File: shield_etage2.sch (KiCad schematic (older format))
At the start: 8 parts, among them J1 Conn_01x02, J2 Conn_01x02

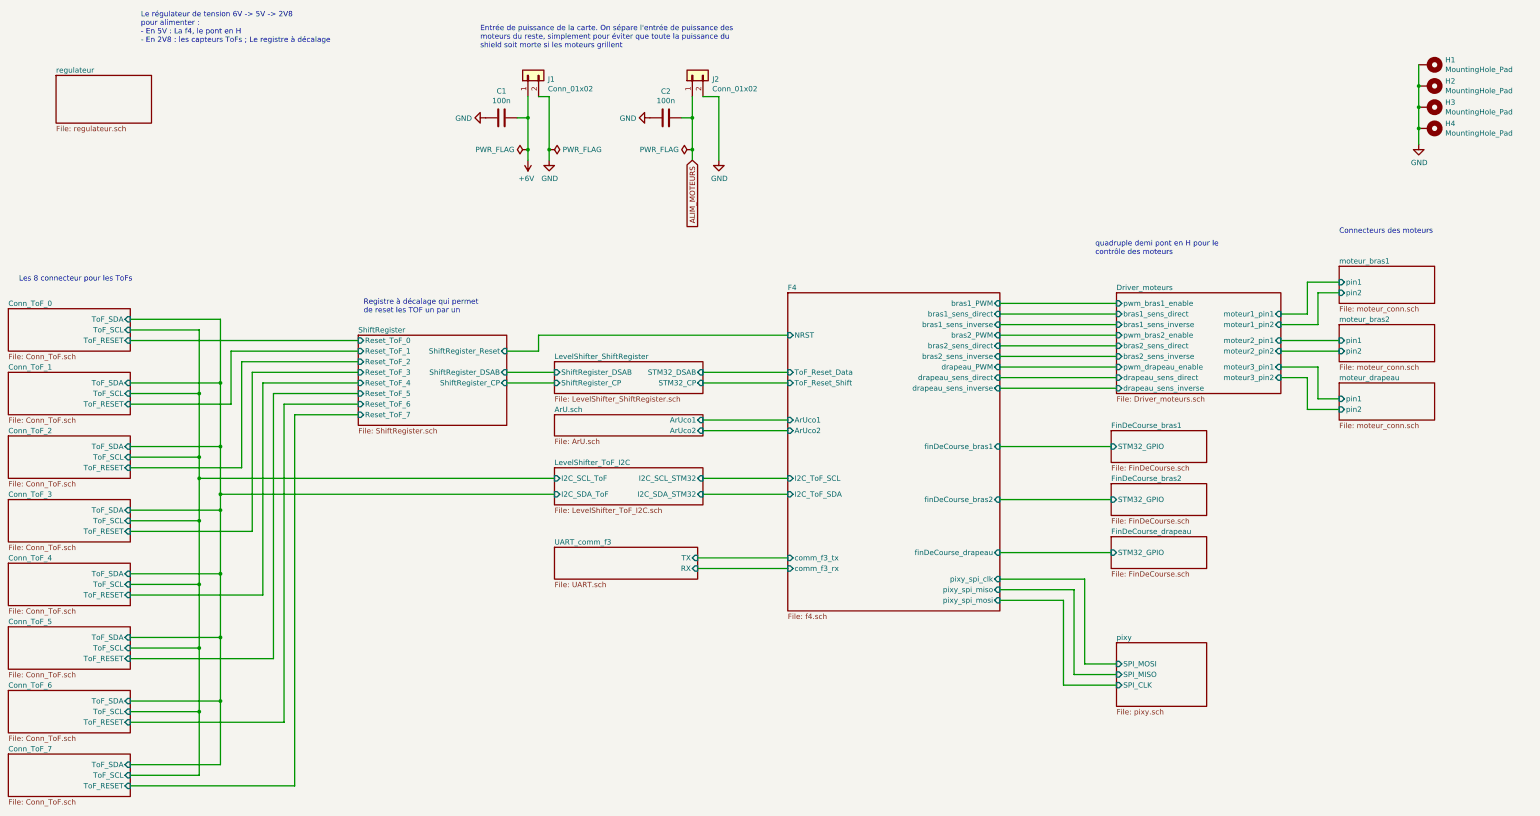
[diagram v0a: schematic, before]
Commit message: removed psi-things pins, added transceiver MCP2551 for CAN, changed motors input protocol, RS must be chosen 1 or 10 kohms, and a foot print for a potentitial 120 ohms resistor is present for CAN bus end.
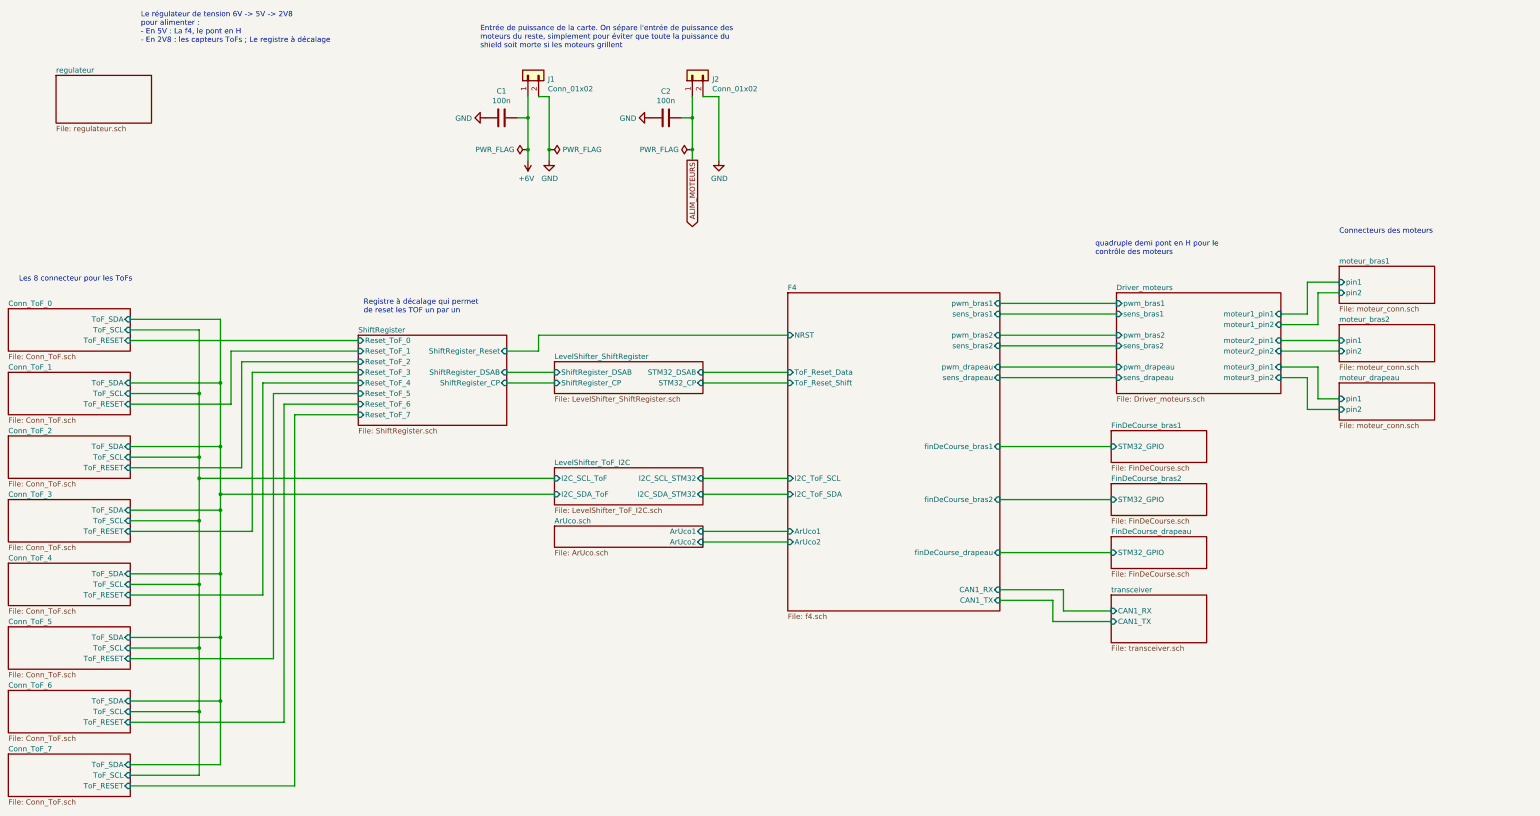
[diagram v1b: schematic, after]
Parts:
- removed H1, H2, H3, H4: MountingHole_Pad, MountingHole:MountingHole_2.2mm_M2_Pad, symbol shield_etage2-rescue:MountingHole_Pad-Mechanical-shield_etage2-rescue
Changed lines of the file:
@@
 $Descr A3 16535 11693
 encoding utf-8
-Sheet 1 24
+Sheet 1 23
 Title ""
 Date ""
@@
 	0    -1   -1   0
 $EndComp
-Text GLabel 7850 3150 3    50   Input ~ 0
+Text GLabel 7850 3150 3    50   Output ~ 0
 ALIM_MOTEURS
 $Comp
@@
 F0 "Driver_moteurs" 50
 F1 "Driver_moteurs.sch" 50
-F2 "bras1_sens_direct" I L 11850 4600 50
-F3 "bras1_sens_inverse" I L 11850 4700 50
-F4 "drapeau_sens_direct" I L 11850 5200 50
-F5 "drapeau_sens_inverse" I L 11850 5300 50
-F6 "moteur1_pin1" I R 13400 4600 50
-F7 "moteur2_pin2" I R 13400 4950 50
-F8 "moteur1_pin2" I R 13400 4700 50
-F9 "moteur2_pin1" I R 13400 4850 50
-F10 "pwm_bras1_enable" I L 11850 4500 50
-F11 "pwm_drapeau_enable" I L 11850 5100 50
-F12 "bras2_sens_direct" I L 11850 4900 50
-F13 "bras2_sens_inverse" I L 11850 5000 50
-F14 "moteur3_pin1" I R 13400 5100 50
-F15 "moteur3_pin2" I R 13400 5200 50
-F16 "pwm_bras2_enable" I L 11850 4800 50
+F2 "sens_bras1" I L 11850 4600 50
+F3 "sens_drapeau" I L 11850 5200 50
+F4 "moteur1_pin1" I R 13400 4600 50
+F5 "moteur2_pin2" I R 13400 4950 50
+F6 "moteur1_pin2" I R 13400 4700 50
+F7 "moteur2_pin1" I R 13400 4850 50
+F8 "pwm_bras1" I L 11850 4500 50
+F9 "pwm_drapeau" I L 11850 5100 50
+F10 "sens_bras2" I L 11850 4900 50
+F11 "moteur3_pin1" I R 13400 5100 50
+F12 "moteur3_pin2" I R 13400 5200 50
+F13 "pwm_bras2" I L 11850 4800 50
 $EndSheet
 Text Notes 11650 4050 0    50   ~ 0
@@
 F2 "STM32_GPIO" I L 11800 5850 50
 $EndSheet
-$Sheet
-S 11850 7700 850  600
-U 5E845744
-F0 "pixy" 50
-F1 "pixy.sch" 50
-F2 "SPI_MOSI" I L 11850 7900 50
-F3 "SPI_MISO" I L 11850 8000 50
-F4 "SPI_CLK" I L 11850 8100 50
-$EndSheet
-$Comp
-L shield_etage2-rescue:MountingHole_Pad-Mechanical-shield_etage2-rescue H1
-U 1 1 5E81B7D6
-P 14800 2250
-F 0 "H1" V 14754 2400 50  0000 L CNN
-F 1 "MountingHole_Pad" V 14845 2400 50  0000 L CNN
-F 2 "MountingHole:MountingHole_2.2mm_M2_Pad" H 14800 2250 50  0001 C CNN
-F 3 "~" H 14800 2250 50  0001 C CNN
-	1    14800 2250
-	0    1    1    0
-$EndComp
-$Comp
-L shield_etage2-rescue:MountingHole_Pad-Mechanical-shield_etage2-rescue H2
-U 1 1 5E81C6C2
-P 14800 2450
-F 0 "H2" V 14754 2600 50  0000 L CNN
-F 1 "MountingHole_Pad" V 14845 2600 50  0000 L CNN
-F 2 "MountingHole:MountingHole_2.2mm_M2_Pad" H 14800 2450 50  0001 C CNN
-F 3 "~" H 14800 2450 50  0001 C CNN
-	1    14800 2450
-	0    1    1    0
-$EndComp
-$Comp
-L shield_etage2-rescue:MountingHole_Pad-Mechanical-shield_etage2-rescue H3
-U 1 1 5E81F44B
-P 14800 2650
-F 0 "H3" V 14754 2800 50  0000 L CNN
-F 1 "MountingHole_Pad" V 14845 2800 50  0000 L CNN
-F 2 "MountingHole:MountingHole_2.2mm_M2_Pad" H 14800 2650 50  0001 C CNN
-F 3 "~" H 14800 2650 50  0001 C CNN
-	1    14800 2650
-	0    1    1    0
-$EndComp
-$Comp
-L shield_etage2-rescue:MountingHole_Pad-Mechanical-shield_etage2-rescue H4
-U 1 1 5E81F451
-P 14800 2850
-F 0 "H4" V 14754 3000 50  0000 L CNN
-F 1 "MountingHole_Pad" V 14845 3000 50  0000 L CNN
-F 2 "MountingHole:MountingHole_2.2mm_M2_Pad" H 14800 2850 50  0001 C CNN
-F 3 "~" H 14800 2850 50  0001 C CNN
-	1    14800 2850
-	0    1    1    0
-$EndComp
-Wire Wire Line
-	14700 2250 14700 2450
-Wire Wire Line
-	14700 2450 14700 2650
-Connection ~ 14700 2450
-Wire Wire Line
-	14700 2650 14700 2850
-Connection ~ 14700 2650
-Connection ~ 14700 2850
-Wire Wire Line
-	14700 2850 14700 3000
-$Comp
-L shield_etage2-rescue:GND-power-shield_etage2-rescue #PWR06
-U 1 1 5E82CE64
-P 14700 3000
-F 0 "#PWR06" H 14700 2750 50  0001 C CNN
-F 1 "GND" H 14705 2827 50  0000 C CNN
-F 2 "" H 14700 3000 50  0001 C CNN
-F 3 "" H 14700 3000 50  0001 C CNN
-	1    14700 3000
-	1    0    0    -1
-$EndComp
 Wire Wire Line
 	6300 2750 6300 3050
@@
 Text Notes 5850 2100 0    50   ~ 0
 Entrée de puissance de la carte. On sépare l'entrée de puissance des\nmoteurs du reste, simplement pour éviter que toute la puissance du\nshield soit morte si les moteurs grillent
-$Sheet
-S 6550 6800 1350 300
-U 5E87EAD4
-F0 "UART_comm_f3" 50
-F1 "UART.sch" 50
-F2 "TX" I R 7900 6900 50
-F3 "RX" I R 7900 7000 50
-$EndSheet
-Wire Wire Line
-	7900 6900 8750 6900
-Wire Wire Line
-	8750 7000 7900 7000
 Wire Wire Line
 	6500 2550 6500 3050
@@
 F7 "finDeCourse_bras1" I R 10750 5850 50
 F8 "finDeCourse_drapeau" I R 10750 6850 50
-F9 "pixy_spi_clk" I R 10750 7100 50
-F10 "pixy_spi_miso" I R 10750 7200 50
-F11 "pixy_spi_mosi" I R 10750 7300 50
-F12 "drapeau_sens_direct" I R 10750 5200 50
-F13 "bras1_sens_direct" I R 10750 4600 50
-F14 "drapeau_sens_inverse" I R 10750 5300 50
-F15 "bras1_sens_inverse" I R 10750 4700 50
-F16 "drapeau_PWM" I R 10750 5100 50
-F17 "comm_f3_tx" I L 8750 6900 50
-F18 "comm_f3_rx" I L 8750 7000 50
-F19 "bras2_PWM" I R 10750 4800 50
-F20 "bras1_PWM" I R 10750 4500 50
-F21 "bras2_sens_direct" I R 10750 4900 50
-F22 "bras2_sens_inverse" I R 10750 5000 50
-F23 "finDeCourse_bras2" I R 10750 6350 50
-F24 "ArUco1" I L 8750 5600 50
-F25 "ArUco2" I L 8750 5700 50
+F9 "sens_drapeau" I R 10750 5200 50
+F10 "sens_bras1" I R 10750 4600 50
+F11 "pwm_drapeau" I R 10750 5100 50
+F12 "pwm_bras2" I R 10750 4800 50
+F13 "pwm_bras1" I R 10750 4500 50
+F14 "sens_bras2" I R 10750 4900 50
+F15 "finDeCourse_bras2" I R 10750 6350 50
+F16 "ArUco1" I L 8750 6650 50
+F17 "ArUco2" I L 8750 6750 50
+F18 "CAN1_RX" I R 10750 7200 50
+F19 "CAN1_TX" I R 10750 7300 50
 $EndSheet
 Wire Wire Line
@@
 	10750 4600 11850 4600
 Wire Wire Line
-	11850 4700 10750 4700
-Wire Wire Line
 	10750 4800 11850 4800
 Wire Wire Line
 	11850 4900 10750 4900
 Wire Wire Line
-	10750 5000 11850 5000
-Wire Wire Line
 	11850 5100 10750 5100
 Wire Wire Line
 	10750 5200 11850 5200
-Wire Wire Line
-	11850 5300 10750 5300
 Wire Wire Line
 	13400 4850 13950 4850
@@
 	11800 6350 10750 6350
 Wire Wire Line
-	11850 7900 11550 7900
-Wire Wire Line
-	11550 7900 11550 7100
-Wire Wire Line
-	11550 7100 10750 7100
-Wire Wire Line
-	10750 7200 11450 7200
-Wire Wire Line
-	11450 7200 11450 8000
-Wire Wire Line
-	11450 8000 11850 8000
-Wire Wire Line
-	11850 8100 11350 8100
-Wire Wire Line
-	11350 8100 11350 7300
-Wire Wire Line
-	11350 7300 10750 7300
-$Sheet
-S 6550 5550 1400 200
+	8750 6650 7950 6650
+Wire Wire Line
+	8750 6750 7950 6750
+$Sheet
+S 6550 6600 1400 200
 U 5F81CFC3
-F0 "ArU.sch" 50
-F1 "ArU.sch" 50
-F2 "ArUco1" I R 7950 5600 50
-F3 "ArUco2" I R 7950 5700 50
-$EndSheet
-Wire Wire Line
-	8750 5600 7950 5600
-Wire Wire Line
-	8750 5700 7950 5700
+F0 "ArUco.sch" 50
+F1 "ArUco.sch" 50
+F2 "ArUco1" I R 7950 6650 50
+F3 "ArUco2" I R 7950 6750 50
+$EndSheet
+$Sheet
+S 11800 7250 900  450
+U 5F844B5D
+F0 "transceiver" 50
+F1 "transceiver.sch" 50
+F2 "CAN1_RX" I L 11800 7400 50
+F3 "CAN1_TX" I L 11800 7500 50
+$EndSheet
+Wire Wire Line
+	11350 7200 11350 7400
+Wire Wire Line
+	11350 7400 11800 7400
+Wire Wire Line
+	10750 7200 11350 7200
+Wire Wire Line
+	11250 7500 11250 7300
+Wire Wire Line
+	11250 7300 10750 7300
+Wire Wire Line
+	11250 7500 11800 7500
 $EndSCHEMATC
